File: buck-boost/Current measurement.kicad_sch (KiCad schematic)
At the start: 15 parts, among them U3 ACS730xLCTR-20AB, U8 ACS730xLCTR-20AB, U9 ACS730xLCTR-20AB

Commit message: Editing sheets(Power labels, sheet color, adding text), Adding information in the sensor sheets
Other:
- removed sheet Signal conditioning
- removed sheet Signal conditioning1
- removed sheet Signal conditioning2
- added sheet Signal conditioning6 (Signal conditioning10.kicad_sch)
- added sheet Signal conditioning7 (Signal conditioning10.kicad_sch)
- added sheet Signal conditioning8 (Signal conditioning10.kicad_sch)
- note added: "change labels power"
- note added: "indcutor current take specially care measurimg imductor current (ACS730xLCTR-20AB) in out current ACS712x(LCTR-20AB)(cheaper)"
- note removed: "change the color"

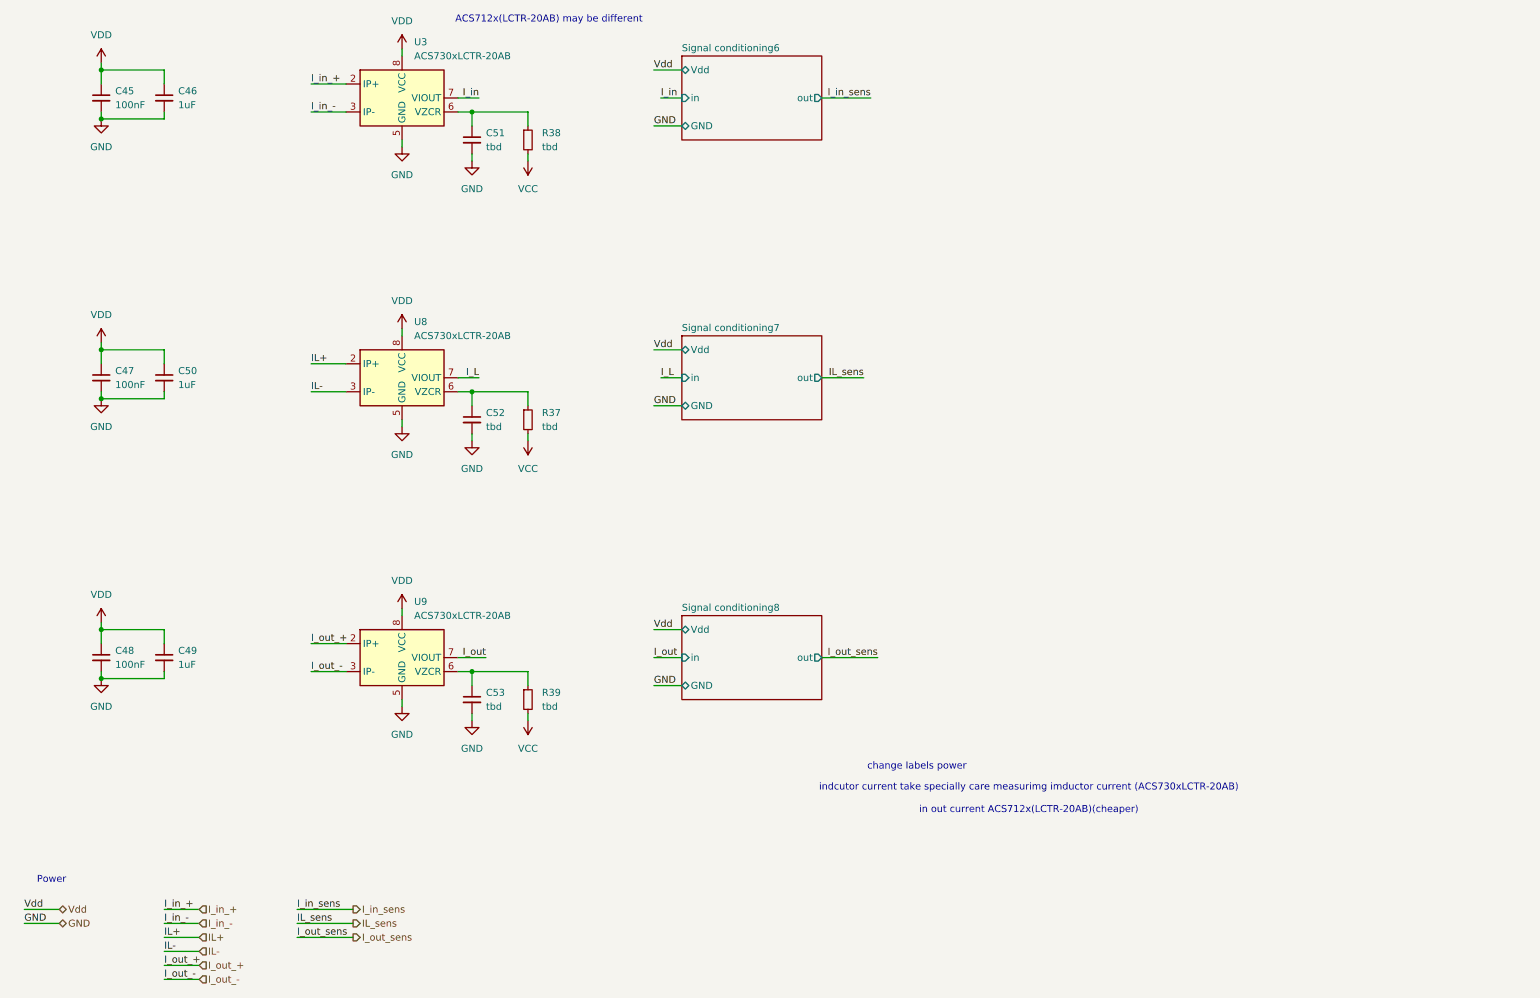
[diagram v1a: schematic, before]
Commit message: Adding supply block
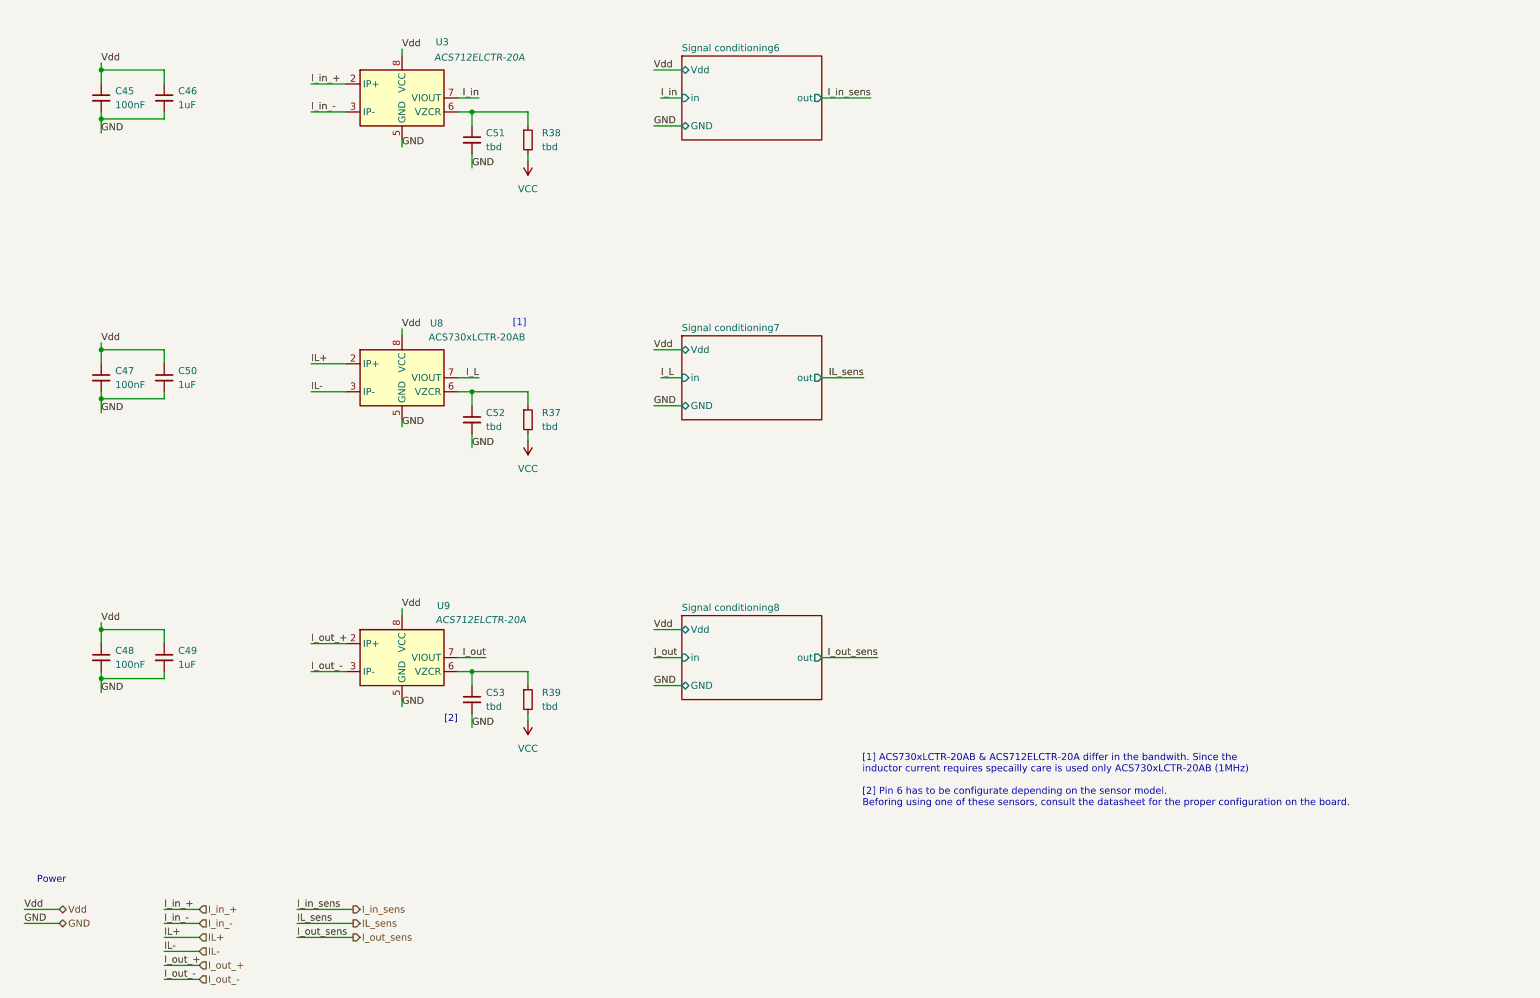
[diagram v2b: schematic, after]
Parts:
- U3, U9: value ACS730xLCTR-20AB -> ACS712ELCTR-20A
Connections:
- net VDD is gone; now on net Vdd: C45.1, C46.1, C47.1, C48.1, C49.1, C50.1, U3.8 (VCC), U8.8 (VCC), U9.8 (VCC)
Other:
- note added: "[1]"
- note added: "[1] ACS730xLCTR-20AB & ACS712ELCTR-20A differ in the bandwith. Since the inductor current requires specailly care is used only ACS730xLCTR-20AB (1MHz) [2] Pin 6 has to be configurate depending on the sensor model. Beforing using one of these sensors, consult the datasheet for the proper configuration on the board."
- note added: "[2]"
- note removed: "ACS712x(LCTR-20AB) may be different"
- note removed: "change labels power"
- note removed: "indcutor current take specially care measurimg imductor current (ACS730xLCTR-20AB) in out current ACS712x(LCTR-20AB)(cheaper)"

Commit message: The changes indicated in the text document Review. 05.11.2024 were implemented. Missing footprints were added
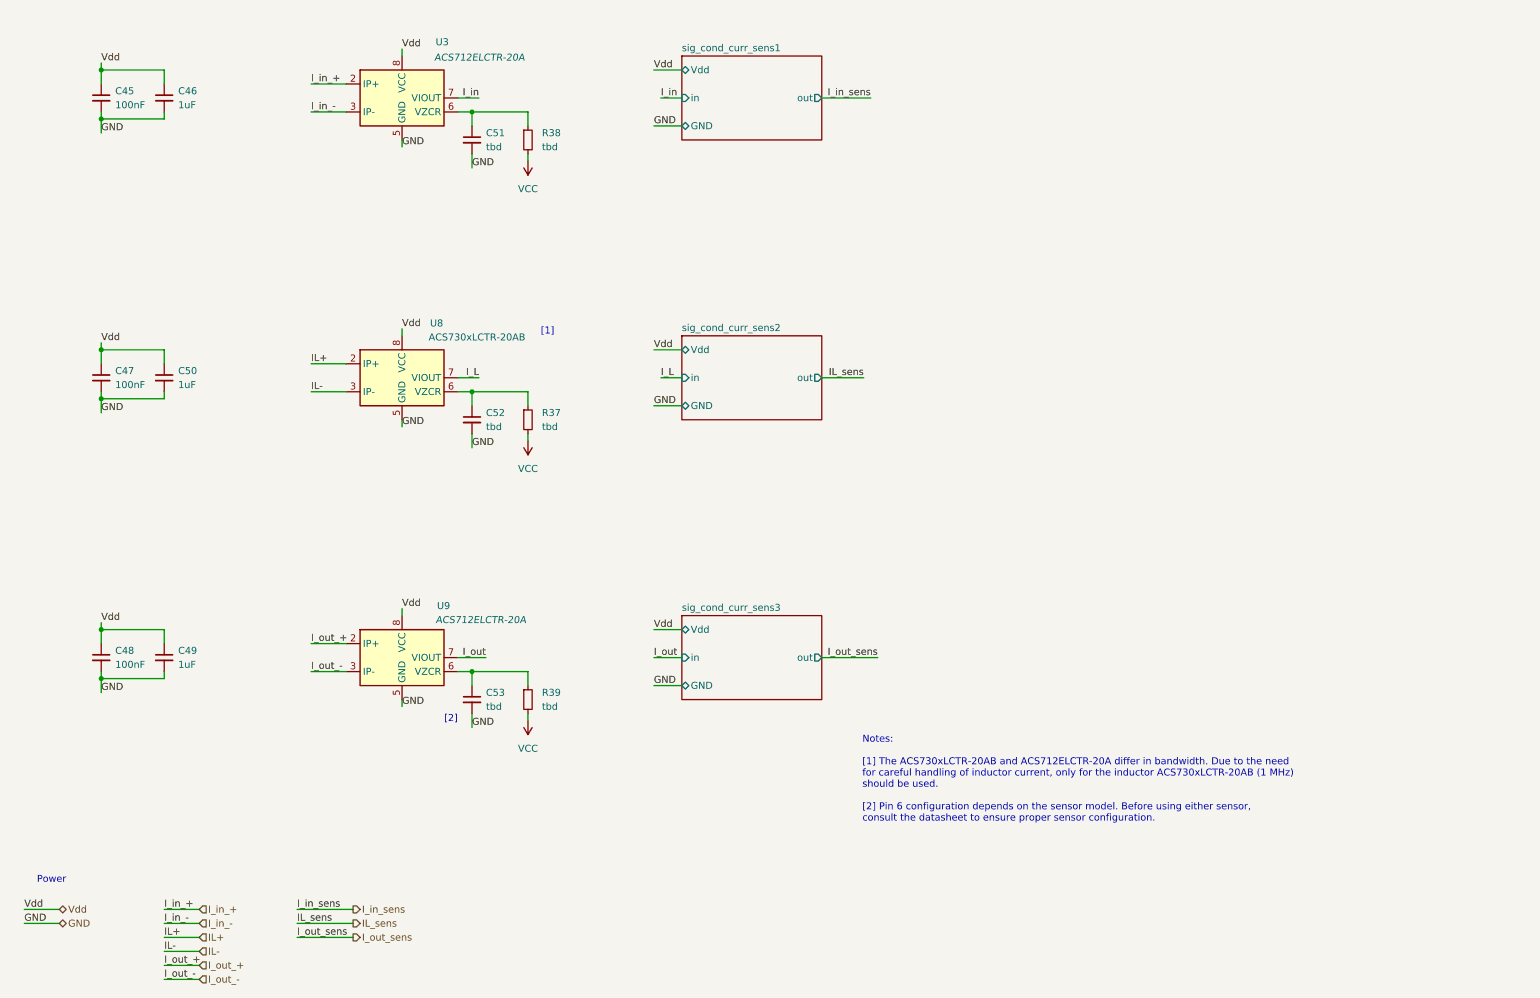
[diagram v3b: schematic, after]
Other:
- sheet Signal conditioning6 renamed sig_cond_curr_sens1
- sheet Signal conditioning7 renamed sig_cond_curr_sens2
- sheet Signal conditioning8 renamed sig_cond_curr_sens3
- sheet sig_cond_curr_sens1: file Signal conditioning10.kicad_sch -> Signal conditioning_Current.kicad_sch
- sheet sig_cond_curr_sens2: file Signal conditioning10.kicad_sch -> Signal conditioning_Current.kicad_sch
- sheet sig_cond_curr_sens3: file Signal conditioning10.kicad_sch -> Signal conditioning_Current.kicad_sch
- note added: "Notes: [1] The ACS730xLCTR-20AB and ACS712ELCTR-20A differ in bandwidth. Due to the need for careful handling of inductor current, only for the inductor ACS730xLCTR-20AB (1 MHz) should be used. [2] Pin 6 configuration depends on the sensor model. Before using either sensor, consult the datasheet to ensure proper sensor configuration."
- note removed: "[1] ACS730xLCTR-20AB & ACS712ELCTR-20A differ in the bandwith. Since the inductor current requires specailly care is used only ACS730xLCTR-20AB (1MHz) [2] Pin 6 has to be configurate depending on the sensor model. Beforing using one of these sensors, consult the datasheet for the proper configuration on the board."
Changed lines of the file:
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@@
 		)
 	)
-	(text "[1] ACS730xLCTR-20AB & ACS712ELCTR-20A differ in the bandwith. Since the \ninductor current requires specailly care is used only ACS730xLCTR-20AB (1MHz)\n\n[2] Pin 6 has to be configurate depending on the sensor model.\nBeforing using one of these sensors, consult the datasheet for the proper configuration on the board."
+	(text "Notes:\n\n[1] The ACS730xLCTR-20AB and ACS712ELCTR-20A differ in bandwidth. Due to the need\nfor careful handling of inductor current, only for the inductor ACS730xLCTR-20AB (1 MHz)\nshould be used.\n\n[2] Pin 6 configuration depends on the sensor model. Before using either sensor,\nconsult the datasheet to ensure proper sensor configuration."
 		(exclude_from_sim no)
-		(at 177.546 154.432 0)
+		(at 177.546 154.178 0)
 		(effects
 			(font
@@
 	(text "[1]"
 		(exclude_from_sim no)
-		(at 115.316 71.374 0)
+		(at 120.396 72.898 0)
 		(effects
 			(font
@@
 			(color 255 253 231 1.0000)
 		)
-		(property "Sheetname" "Signal conditioning6"
+		(property "Sheetname" "sig_cond_curr_sens1"
 			(at 144.78 22.1484 0)
 			(effects
@@
 			)
 		)
-		(property "Sheetfile" "Signal conditioning10.kicad_sch"
+		(property "Sheetfile" "Signal conditioning_Current.kicad_sch"
 			(at 144.78 38.6846 0)
 			(effects
@@
 			(color 255 253 231 1.0000)
 		)
-		(property "Sheetname" "Signal conditioning7"
+		(property "Sheetname" "sig_cond_curr_sens2"
 			(at 144.78 72.9484 0)
 			(effects
@@
 			)
 		)
-		(property "Sheetfile" "Signal conditioning10.kicad_sch"
+		(property "Sheetfile" "Signal conditioning_Current.kicad_sch"
 			(at 144.78 89.4846 0)
 			(effects
@@
 			(color 255 253 231 1.0000)
 		)
-		(property "Sheetname" "Signal conditioning8"
+		(property "Sheetname" "sig_cond_curr_sens3"
 			(at 144.78 123.7484 0)
 			(effects
@@
 			)
 		)
-		(property "Sheetfile" "Signal conditioning10.kicad_sch"
+		(property "Sheetfile" "Signal conditioning_Current.kicad_sch"
 			(at 144.78 140.2846 0)
 			(effects
